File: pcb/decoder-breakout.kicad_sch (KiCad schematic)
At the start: 18 parts, among them J1 SM04B-SRSS-TB_LF__SN_, J2 SM04B-SRSS-TB_LF__SN_, J3 TBL009-254-08GY-2GY, Q1 BSS138, Q2 BSS138, U1 LS7866-S

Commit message: corrected jumper wiring
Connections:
- net VDD: no longer JP3.2 (B), JP4.2 (B), JP5.2 (B)
- net at R5.1, U1.10 (A2): now also JP5.2 (B)
- net at R3.1, U1.8 (A0): now also JP3.2 (B)
- net at R4.1, U1.9 (A1): now also JP4.2 (B)
- no-connect marks 0 -> 2
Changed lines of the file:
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@@
 (kicad_sch (version 20230121) (generator eeschema)
   (paper "A4")
-  (junction (at 104.14 101.6) (diameter 0) (color 0 0 0 0)
-  )
   (junction (at 182.88 76.2) (diameter 0) (color 0 0 0 0)
   )
   (junction (at 167.64 76.2) (diameter 0) (color 0 0 0 0)
   )
+  (junction (at 163.83 106.68) (diameter 0) (color 0 0 0 0)
+  )
   (junction (at 113.03 171.45) (diameter 0) (color 0 0 0 0)
   )
-  (junction (at 104.14 120.65) (diameter 0) (color 0 0 0 0)
-  )
   (junction (at 113.03 152.4) (diameter 0) (color 0 0 0 0)
   )
+  (junction (at 119.38 120.65) (diameter 0) (color 0 0 0 0)
+  )
   (junction (at 199.39 157.48) (diameter 0) (color 0 0 0 0)
   )
@@
   (junction (at 139.7 171.45) (diameter 0) (color 0 0 0 0)
   )
-  (junction (at 104.14 111.76) (diameter 0) (color 0 0 0 0)
+  (junction (at 162.56 76.2) (diameter 0) (color 0 0 0 0)
+  )
+  (junction (at 119.38 101.6) (diameter 0) (color 0 0 0 0)
   )
   (junction (at 172.72 157.48) (diameter 0) (color 0 0 0 0)
@@
   (junction (at 185.42 93.98) (diameter 0) (color 0 0 0 0)
   )
+  (junction (at 119.38 111.76) (diameter 0) (color 0 0 0 0)
+  )
+  (no_connect (at 161.29 86.36))
+  (no_connect (at 161.29 81.28))
   (wire (pts (xy 165.1 157.48) (xy 172.72 157.48))
     (stroke (width 0) (type default))
@@
     (stroke (width 0) (type default))
   )
-  (wire (pts (xy 107.95 111.76) (xy 104.14 111.76))
+  (wire (pts (xy 73.66 111.76) (xy 107.95 111.76))
     (stroke (width 0) (type default))
   )
@@
     (stroke (width 0) (type default))
   )
+  (wire (pts (xy 119.38 104.14) (xy 119.38 101.6))
+    (stroke (width 0) (type default))
+  )
   (wire (pts (xy 182.88 76.2) (xy 182.88 59.69))
     (stroke (width 0) (type default))
@@
     (stroke (width 0) (type default))
   )
+  (wire (pts (xy 119.38 120.65) (xy 128.27 120.65))
+    (stroke (width 0) (type default))
+  )
   (wire (pts (xy 113.03 152.4) (xy 113.03 160.02))
     (stroke (width 0) (type default))
@@
     (stroke (width 0) (type default))
   )
+  (wire (pts (xy 163.83 106.68) (xy 165.1 106.68))
+    (stroke (width 0) (type default))
+  )
   (wire (pts (xy 123.19 101.6) (xy 123.19 93.98))
     (stroke (width 0) (type default))
   )
-  (wire (pts (xy 104.14 111.76) (xy 104.14 114.3))
-    (stroke (width 0) (type default))
-  )
-  (wire (pts (xy 115.57 101.6) (xy 123.19 101.6))
+  (wire (pts (xy 119.38 101.6) (xy 123.19 101.6))
+    (stroke (width 0) (type default))
+  )
+  (wire (pts (xy 115.57 101.6) (xy 119.38 101.6))
     (stroke (width 0) (type default))
   )
@@
     (stroke (width 0) (type default))
   )
-  (wire (pts (xy 104.14 111.76) (xy 73.66 111.76))
-    (stroke (width 0) (type default))
-  )
   (wire (pts (xy 187.96 64.77) (xy 198.12 64.77))
     (stroke (width 0) (type default))
@@
     (stroke (width 0) (type default))
   )
-  (wire (pts (xy 161.29 106.68) (xy 165.1 106.68))
+  (wire (pts (xy 161.29 106.68) (xy 163.83 106.68))
     (stroke (width 0) (type default))
   )
@@
     (stroke (width 0) (type default))
   )
+  (wire (pts (xy 104.14 114.3) (xy 119.38 114.3))
+    (stroke (width 0) (type default))
+  )
   (wire (pts (xy 172.72 157.48) (xy 181.61 157.48))
     (stroke (width 0) (type default))
   )
-  (wire (pts (xy 161.29 76.2) (xy 167.64 76.2))
+  (wire (pts (xy 161.29 76.2) (xy 162.56 76.2))
     (stroke (width 0) (type default))
   )
@@
     (stroke (width 0) (type default))
   )
-  (wire (pts (xy 104.14 120.65) (xy 73.66 120.65))
+  (wire (pts (xy 104.14 104.14) (xy 119.38 104.14))
+    (stroke (width 0) (type default))
+  )
+  (wire (pts (xy 162.56 76.2) (xy 167.64 76.2))
     (stroke (width 0) (type default))
   )
@@
     (stroke (width 0) (type default))
   )
-  (wire (pts (xy 104.14 120.65) (xy 104.14 123.19))
-    (stroke (width 0) (type default))
-  )
   (wire (pts (xy 105.41 171.45) (xy 113.03 171.45))
     (stroke (width 0) (type default))
   )
-  (wire (pts (xy 125.73 111.76) (xy 115.57 111.76))
+  (wire (pts (xy 125.73 111.76) (xy 119.38 111.76))
     (stroke (width 0) (type default))
   )
@@
     (stroke (width 0) (type default))
   )
-  (wire (pts (xy 107.95 101.6) (xy 104.14 101.6))
-    (stroke (width 0) (type default))
-  )
-  (wire (pts (xy 115.57 120.65) (xy 128.27 120.65))
+  (wire (pts (xy 104.14 123.19) (xy 119.38 123.19))
+    (stroke (width 0) (type default))
+  )
+  (wire (pts (xy 73.66 101.6) (xy 107.95 101.6))
+    (stroke (width 0) (type default))
+  )
+  (wire (pts (xy 115.57 120.65) (xy 119.38 120.65))
     (stroke (width 0) (type default))
   )
@@
     (stroke (width 0) (type default))
   )
-  (wire (pts (xy 104.14 101.6) (xy 104.14 104.14))
-    (stroke (width 0) (type default))
-  )
   (wire (pts (xy 139.7 146.05) (xy 139.7 160.02))
     (stroke (width 0) (type default))
@@
     (stroke (width 0) (type default))
   )
+  (wire (pts (xy 119.38 123.19) (xy 119.38 120.65))
+    (stroke (width 0) (type default))
+  )
+  (wire (pts (xy 119.38 111.76) (xy 115.57 111.76))
+    (stroke (width 0) (type default))
+  )
   (wire (pts (xy 130.81 96.52) (xy 125.73 96.52))
     (stroke (width 0) (type default))
@@
     (stroke (width 0) (type default))
   )
-  (wire (pts (xy 107.95 120.65) (xy 104.14 120.65))
+  (wire (pts (xy 119.38 114.3) (xy 119.38 111.76))
+    (stroke (width 0) (type default))
+  )
+  (wire (pts (xy 73.66 120.65) (xy 107.95 120.65))
     (stroke (width 0) (type default))
   )
   (wire (pts (xy 96.52 88.9) (xy 130.81 88.9))
-    (stroke (width 0) (type default))
-  )
-  (wire (pts (xy 104.14 101.6) (xy 73.66 101.6))
     (stroke (width 0) (type default))
   )
@@
     )
   )
-  (global_label "GND" (shape input) (at 195.58 110.49 180) (fields_autoplaced)
-    (effects (font (size 1.27 1.27)) (justify right))
-    (property "Intersheetrefs" "${INTERSHEET_REFS}" (at 188.7243 110.49 0)
-      (effects (font (size 1.27 1.27)) (justify right) hide)
-    )
-  )
   (global_label "VDD" (shape input) (at 172.72 129.54 90) (fields_autoplaced)
     (effects (font (size 1.27 1.27)) (justify left))
@@
     )
   )
+  (global_label "GND" (shape input) (at 195.58 110.49 180) (fields_autoplaced)
+    (effects (font (size 1.27 1.27)) (justify right))
+    (property "Intersheetrefs" "${INTERSHEET_REFS}" (at 188.7243 110.49 0)
+      (effects (font (size 1.27 1.27)) (justify right) hide)
+    )
+  )
   (symbol (lib_id "power:GND") (at 165.1 110.49 0) (unit 1)
     (in_bom yes) (on_board yes) (dnp no) (fields_autoplaced)
@@
   (symbol (lib_id "Device:R_US") (at 111.76 120.65 270) (unit 1)
     (in_bom yes) (on_board yes) (dnp no)
-    (property "Reference" "R5" (at 111.76 123.19 90)
-      (effects (font (size 1.27 1.27)))
-    )
-    (property "Value" "300" (at 111.76 125.73 90)
+    (property "Reference" "R5" (at 111.76 115.57 90)
+      (effects (font (size 1.27 1.27)))
+    )
+    (property "Value" "300" (at 111.76 118.11 90)
       (effects (font (size 1.27 1.27)))
     )
@@
     )
   )
+  (symbol (lib_id "power:PWR_FLAG") (at 163.83 106.68 0) (unit 1)
+    (in_bom yes) (on_board yes) (dnp no) (fields_autoplaced)
+    (property "Reference" "#FLG01" (at 163.83 104.775 0)
+      (effects (font (size 1.27 1.27)) hide)
+    )
+    (property "Value" "PWR_FLAG" (at 163.83 101.6 0)
+      (effects (font (size 1.27 1.27)))
+    )
+    (property "Footprint" "" (at 163.83 106.68 0)
+      (effects (font (size 1.27 1.27)) hide)
+    )
+    (property "Datasheet" "~" (at 163.83 106.68 0)
+      (effects (font (size 1.27 1.27)) hide)
+    )
+    (pin "1")
+    (instances
+      (project "decoder-breakout"
+        (path "/1a0ebad1-ea8c-4043-8a0c-94ccddf3b0fc"
+          (reference "#FLG01") (unit 1)
+        )
+      )
+    )
+  )
   (symbol (lib_id "LS7866-S:LS7866-S") (at 146.05 91.44 0) (unit 1)
     (in_bom yes) (on_board yes) (dnp no) (fields_autoplaced)
@@
   (symbol (lib_id "Device:R_US") (at 111.76 101.6 270) (unit 1)
     (in_bom yes) (on_board yes) (dnp no)
-    (property "Reference" "R3" (at 111.76 104.14 90)
-      (effects (font (size 1.27 1.27)))
-    )
-    (property "Value" "300" (at 111.76 106.68 90)
+    (property "Reference" "R3" (at 111.76 96.52 90)
+      (effects (font (size 1.27 1.27)))
+    )
+    (property "Value" "300" (at 111.76 99.06 90)
       (effects (font (size 1.27 1.27)))
     )
@@
   (symbol (lib_id "Device:R_US") (at 111.76 111.76 270) (unit 1)
     (in_bom yes) (on_board yes) (dnp no)
-    (property "Reference" "R4" (at 111.76 114.3 90)
-      (effects (font (size 1.27 1.27)))
-    )
-    (property "Value" "300" (at 111.76 116.84 90)
+    (property "Reference" "R4" (at 111.76 106.68 90)
+      (effects (font (size 1.27 1.27)))
+    )
+    (property "Value" "300" (at 111.76 109.22 90)
       (effects (font (size 1.27 1.27)))
     )
@@
         )
       )
+    )
+  )
+  (symbol (lib_id "power:PWR_FLAG") (at 162.56 76.2 0) (unit 1)
+    (in_bom yes) (on_board yes) (dnp no) (fields_autoplaced)
+    (property "Reference" "#FLG02" (at 162.56 74.295 0)
+      (effects (font (size 1.27 1.27)) hide)
+    )
+    (property "Value" "PWR_FLAG" (at 162.56 71.12 0)
+      (effects (font (size 1.27 1.27)))
+    )
+    (property "Footprint" "" (at 162.56 76.2 0)
+      (effects (font (size 1.27 1.27)) hide)
+    )
+    (property "Datasheet" "~" (at 162.56 76.2 0)
+      (effects (font (size 1.27 1.27)) hide)
+    )
+    (pin "1")
+    (instances
+      (project "decoder-breakout"
+        (path "/1a0ebad1-ea8c-4043-8a0c-94ccddf3b0fc"
+          (reference "#FLG02") (unit 1)
+        )
+      )

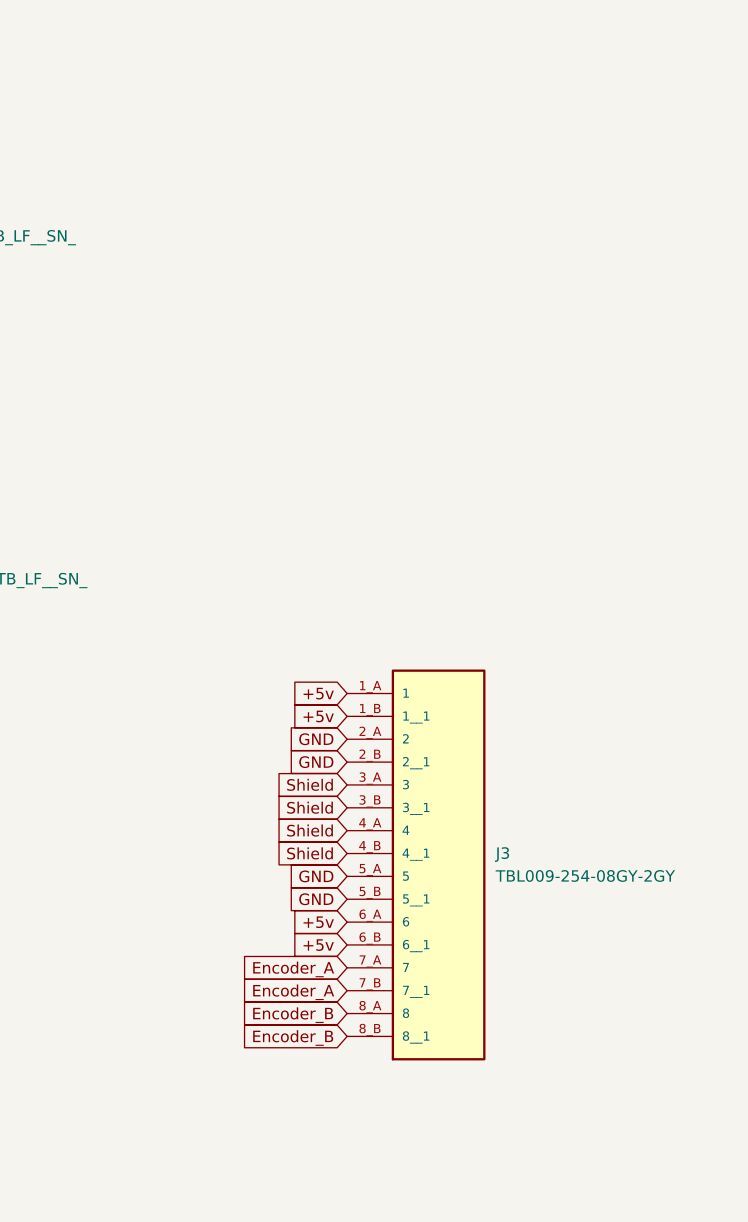
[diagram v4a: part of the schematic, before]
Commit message: clean up terminal block pins
- add 10 and 14 pin terminal blocks for possible use in the future
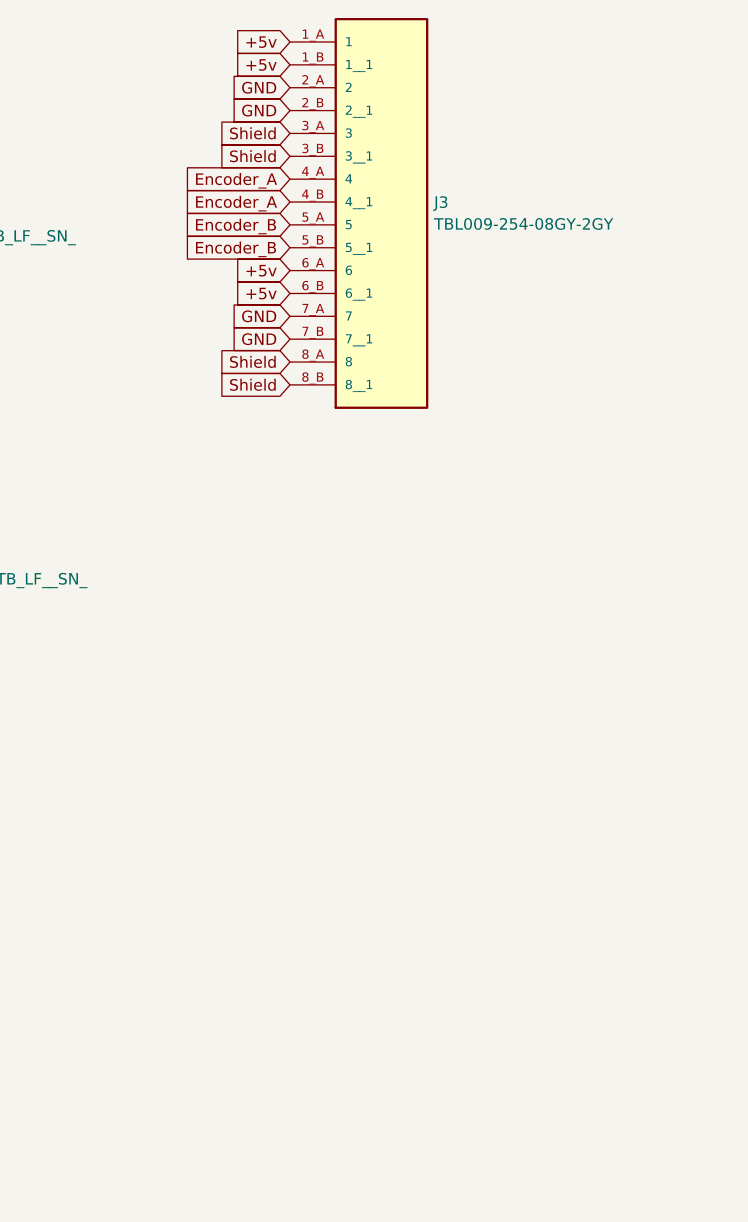
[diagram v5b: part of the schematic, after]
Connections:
- net Encoder_A: now also J3.4_A (4), J3.4_B (4__1); no longer J3.7_A (7), J3.7_B (7__1)
- net Encoder_B: now also J3.5_A (5), J3.5_B (5__1); no longer J3.8_A (8), J3.8_B (8__1)
- net GND: now also J3.7_A (7), J3.7_B (7__1); no longer J3.5_A (5), J3.5_B (5__1)
- net Shield: now also J3.8_A (8), J3.8_B (8__1); no longer J3.4_A (4), J3.4_B (4__1)
